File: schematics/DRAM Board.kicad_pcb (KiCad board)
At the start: 2 copper layers, 114.3 x 53.3 mm, 17 parts, among them U1 AS4C256K16E0, U16 44256_DRAM, U17 44256_DRAM, U18 44256_DRAM, U19 44256_DRAM, U2 AS4C256K16E0, U20 44256_DRAM, U21 44256_DRAM, U22 44256_DRAM, U23 44256_DRAM, U3 AS4C256K16E0, U4 AS4C256K16E0, U5 LM1117-3.3

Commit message: Add files via upload
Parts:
- removed U16, U17, U18, U19, U20, U21, U22, U23: 44256_DRAM, Package_DIP:DIP-20_W7.62mm_Socket
- removed U3, U4: AS4C256K16E0, Package_SO:TSOP-II-40-44_10.16x18.41mm_P0.8mm
- removed U5: LM1117-3.3, Package_TO_SOT_SMD:SOT-223
- added /bras0: Conn_01x01, Connector_PinHeader_2.54mm:PinHeader_1x01_P2.54mm_Vertical, F.Cu at (143.0, 82.1)
- added /bras1: Conn_01x01, Connector_PinHeader_2.54mm:PinHeader_1x01_P2.54mm_Vertical, F.Cu at (230.4, 82.0)
- added /lcas: Conn_01x01, Connector_PinHeader_2.54mm:PinHeader_1x01_P2.54mm_Vertical, F.Cu at (238.0, 82.0)
- added /ucas: Conn_01x01, Connector_PinHeader_2.54mm:PinHeader_1x01_P2.54mm_Vertical, F.Cu at (150.6, 82.1)
- added /we: Conn_01x01, Connector_PinHeader_2.54mm:PinHeader_1x01_P2.54mm_Vertical, F.Cu at (143.0, 79.6)
- added C5: 0.1uF, Capacitor_SMD:C_1206_3216Metric_Pad1.42x1.75mm_HandSolder, F.Cu at (215.9, 97.2)
- added C6: 0.1uF, Capacitor_SMD:C_1206_3216Metric_Pad1.42x1.75mm_HandSolder, F.Cu at (208.9, 80.6)
- added a0: Conn_01x01, Connector_PinHeader_2.54mm:PinHeader_1x01_P2.54mm_Vertical, F.Cu at (143.0, 87.2)
- added a1: Conn_01x01, Connector_PinHeader_2.54mm:PinHeader_1x01_P2.54mm_Vertical, F.Cu at (143.0, 89.7)
- added a2: Conn_01x01, Connector_PinHeader_2.54mm:PinHeader_1x01_P2.54mm_Vertical, F.Cu at (143.0, 92.3)
- added a3: Conn_01x01, Connector_PinHeader_2.54mm:PinHeader_1x01_P2.54mm_Vertical, F.Cu at (143.0, 94.8)
- added a4: Conn_01x01, Connector_PinHeader_2.54mm:PinHeader_1x01_P2.54mm_Vertical, F.Cu at (150.6, 97.3)
- added a5: Conn_01x01, Connector_PinHeader_2.54mm:PinHeader_1x01_P2.54mm_Vertical, F.Cu at (150.6, 94.8)
- added a6: Conn_01x01, Connector_PinHeader_2.54mm:PinHeader_1x01_P2.54mm_Vertical, F.Cu at (150.6, 92.3)
- added a7: Conn_01x01, Connector_PinHeader_2.54mm:PinHeader_1x01_P2.54mm_Vertical, F.Cu at (150.6, 89.7)
- added a8: Conn_01x01, Connector_PinHeader_2.54mm:PinHeader_1x01_P2.54mm_Vertical, F.Cu at (150.6, 87.2)
- added d0: Conn_01x01, Connector_PinHeader_2.54mm:PinHeader_1x01_P2.54mm_Vertical, F.Cu at (238.0, 79.5)
- added d1: Conn_01x01, Connector_PinHeader_2.54mm:PinHeader_1x01_P2.54mm_Vertical, F.Cu at (230.4, 77.0)
- added d10: Conn_01x01, Connector_PinHeader_2.54mm:PinHeader_1x01_P2.54mm_Vertical, F.Cu at (176.0, 77.0)
- added d11: Conn_01x01, Connector_PinHeader_2.54mm:PinHeader_1x01_P2.54mm_Vertical, F.Cu at (168.4, 74.5)
- added d12: Conn_01x01, Connector_PinHeader_2.54mm:PinHeader_1x01_P2.54mm_Vertical, F.Cu at (150.6, 79.6)
- added d13: Conn_01x01, Connector_PinHeader_2.54mm:PinHeader_1x01_P2.54mm_Vertical, F.Cu at (143.0, 77.0)
- added d14: Conn_01x01, Connector_PinHeader_2.54mm:PinHeader_1x01_P2.54mm_Vertical, F.Cu at (150.6, 77.0)
- added d15: Conn_01x01, Connector_PinHeader_2.54mm:PinHeader_1x01_P2.54mm_Vertical, F.Cu at (143.0, 74.5)
- added d2: Conn_01x01, Connector_PinHeader_2.54mm:PinHeader_1x01_P2.54mm_Vertical, F.Cu at (238.0, 77.0)
- added d3: Conn_01x01, Connector_PinHeader_2.54mm:PinHeader_1x01_P2.54mm_Vertical, F.Cu at (230.4, 74.4)
- added d4: Conn_01x01, Connector_PinHeader_2.54mm:PinHeader_1x01_P2.54mm_Vertical, F.Cu at (201.3, 79.5)
- added d5: Conn_01x01, Connector_PinHeader_2.54mm:PinHeader_1x01_P2.54mm_Vertical, F.Cu at (193.7, 76.9)
- added d6: Conn_01x01, Connector_PinHeader_2.54mm:PinHeader_1x01_P2.54mm_Vertical, F.Cu at (201.3, 76.9)
- added d7: Conn_01x01, Connector_PinHeader_2.54mm:PinHeader_1x01_P2.54mm_Vertical, F.Cu at (193.7, 74.4)
- added d8: Conn_01x01, Connector_PinHeader_2.54mm:PinHeader_1x01_P2.54mm_Vertical, F.Cu at (176.0, 79.6)
- added d9: Conn_01x01, Connector_PinHeader_2.54mm:PinHeader_1x01_P2.54mm_Vertical, F.Cu at (168.4, 77.0)
- added gnd_u17: Conn_01x01, Connector_PinHeader_2.54mm:PinHeader_1x01_P2.54mm_Vertical, F.Cu at (201.3, 74.4)
- added gnd_u19: Conn_01x01, Connector_PinHeader_2.54mm:PinHeader_1x01_P2.54mm_Vertical, F.Cu at (150.6, 74.5)
- added gnd_u20: Conn_01x01, Connector_PinHeader_2.54mm:PinHeader_1x01_P2.54mm_Vertical, F.Cu at (238.0, 74.4)
- added gnd_u23: Conn_01x01, Connector_PinHeader_2.54mm:PinHeader_1x01_P2.54mm_Vertical, F.Cu at (162.1, 74.5)
- added vcc_u17: Conn_01x01, Connector_PinHeader_2.54mm:PinHeader_1x01_P2.54mm_Vertical, F.Cu at (193.7, 97.3)
- added vcc_u19: Conn_01x01, Connector_PinHeader_2.54mm:PinHeader_1x01_P2.54mm_Vertical, F.Cu at (143.0, 97.3)
- added vcc_u20: Conn_01x01, Connector_PinHeader_2.54mm:PinHeader_1x01_P2.54mm_Vertical, F.Cu at (230.4, 97.3)
- added vcc_u23: Conn_01x01, Connector_PinHeader_2.54mm:PinHeader_1x01_P2.54mm_Vertical, F.Cu at (154.4, 97.3)
- U1, U2: value AS4C256K16E0 -> IS41C16257; footprint Package_SO:TSOP-II-40-44_10.16x18.41mm_P0.8mm -> Package_SO_J-Lead:SOJ-40
- moved C3 53.1 mm to (168.9, 80.6)
- moved C2 39.6 mm to (175.3, 97.2), turned to 180 degrees
- moved C4 38.6 mm to (209.6, 97.2)
- moved U1 34.1 mm to (172.7, 88.9)
- moved C1 32.8 mm to (168.9, 97.2)
- moved U2 31.8 mm to (213.4, 88.9)
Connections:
- C1 pad 1: /VCC -> /vcc5
- C2 pad 1: /VCC -> /vcc5
- C3 pad 1: /VCC -> /vcc5
- C4 pad 1: /VCC -> /vcc5
- U1 pad 1: /VCC -> /vcc5
- U1 pad 13: Net-(U1-Pad13) -> /_we
- U1 pad 14: Net-(U1-Pad14) -> /_bras0
- U1 pad 15: /_we -> Net-(U1-Pad15)
- U1 pad 16: /_bras0 -> /a0
- U1 pad 17: Net-(U1-Pad17) -> /a1
- U1 pad 18: /a0 -> /a2
- U1 pad 19: /a1 -> /a3
- U1 pad 20: /a2 -> /vcc5
- U1 pad 21: /a3 -> /gnd
- U1 pad 22: /VCC -> /a4
- U1 pad 23: /gnd -> /a5
- U1 pad 24: /a4 -> /a6
- U1 pad 25: /a5 -> /a7
- U1 pad 26: /a6 -> /a8
- U1 pad 27: /a7 -> /gnd
- U1 pad 28: /a8 -> /_ucas
- U1 pad 29: /_oe -> /_lcas
- U1 pad 30: /_ucas -> Net-(U1-Pad30)
- U1 pad 31: /_lcas -> /d8
- U1 pad 32: Net-(U1-Pad32) -> /d9
- U1 pad 35: /d8 -> /gnd
- U1 pad 36: /d9 -> /d12
- U1 pad 37: /d10 -> /d13
- U1 pad 38: /d11 -> /d14
- U1 pad 39: /gnd -> /d15
- U1 pad 40: /d12 -> /gnd
- U1 pad 6: /VCC -> /vcc5
- U2 pad 1: /VCC -> /vcc5
- U2 pad 13: Net-(U2-Pad13) -> /_we
- U2 pad 14: Net-(U2-Pad14) -> /_bras1
- U2 pad 15: /_we -> Net-(U2-Pad15)
- U2 pad 16: /_bras0 -> /a0
- U2 pad 17: Net-(U2-Pad17) -> /a1
- U2 pad 18: /a0 -> /a2
- U2 pad 19: /a1 -> /a3
- U2 pad 20: /a2 -> /vcc5
- U2 pad 21: /a3 -> /gnd
- U2 pad 22: /VCC -> /a4
- U2 pad 23: /gnd -> /a5
- U2 pad 24: /a4 -> /a6
- U2 pad 25: /a5 -> /a7
- U2 pad 26: /a6 -> /a8
- U2 pad 27: /a7 -> /gnd
- U2 pad 28: /a8 -> /_ucas
- U2 pad 29: /_oe -> /_lcas
- U2 pad 30: /_ucas -> Net-(U2-Pad30)
- U2 pad 31: /_lcas -> /d8
- U2 pad 32: Net-(U2-Pad32) -> /d9
- U2 pad 35: /d8 -> /gnd
- U2 pad 36: /d9 -> /d12
- U2 pad 37: /d10 -> /d13
- U2 pad 38: /d11 -> /d14
- U2 pad 39: /gnd -> /d15
- U2 pad 40: /d12 -> /gnd
- U2 pad 6: /VCC -> /vcc5
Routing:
- net /_oe: track 182.9 -> 0.00 mm, vias 3 -> 0
- net /VCC: track 180.0 -> 0.00 mm, vias 5 -> 0
- net /a0: track 223.4 -> 87.9 mm, vias 3 -> 1
- net /a2: track 222.0 -> 88.9 mm, vias 2 -> 1
- net /a8: track 200.2 -> 77.4 mm, vias 3 -> 0
- net /a6: track 202.9 -> 82.0 mm, vias 2 -> 0
- net /a7: track 190.7 -> 79.7 mm, vias 3 -> 0
- net /a5: track 186.9 -> 84.3 mm, vias 5 -> 0
- net /_bras1: track 118.9 -> 18.4 mm, vias 3 -> 0
- net /_we: track 182.4 -> 84.5 mm, vias 4 -> 1
- net /a4: track 180.9 -> 84.8 mm, vias 5 -> 0
- net /gnd: track 292.2 -> 207.3 mm, vias 5 -> 8
- net /_bras0: track 123.7 -> 40.0 mm, vias 3 -> 1
- net /a3: track 222.6 -> 150.8 mm, vias 2 -> 1
- net /d14: track 136.6 -> 76.4 mm, vias 3 -> 1
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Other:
- board size 114.3 x 53.3 mm -> 99.1 x 27.9 mm
- board text added: "IS41C16257"
- board text added: "gnd"
- board text added: "vcc"

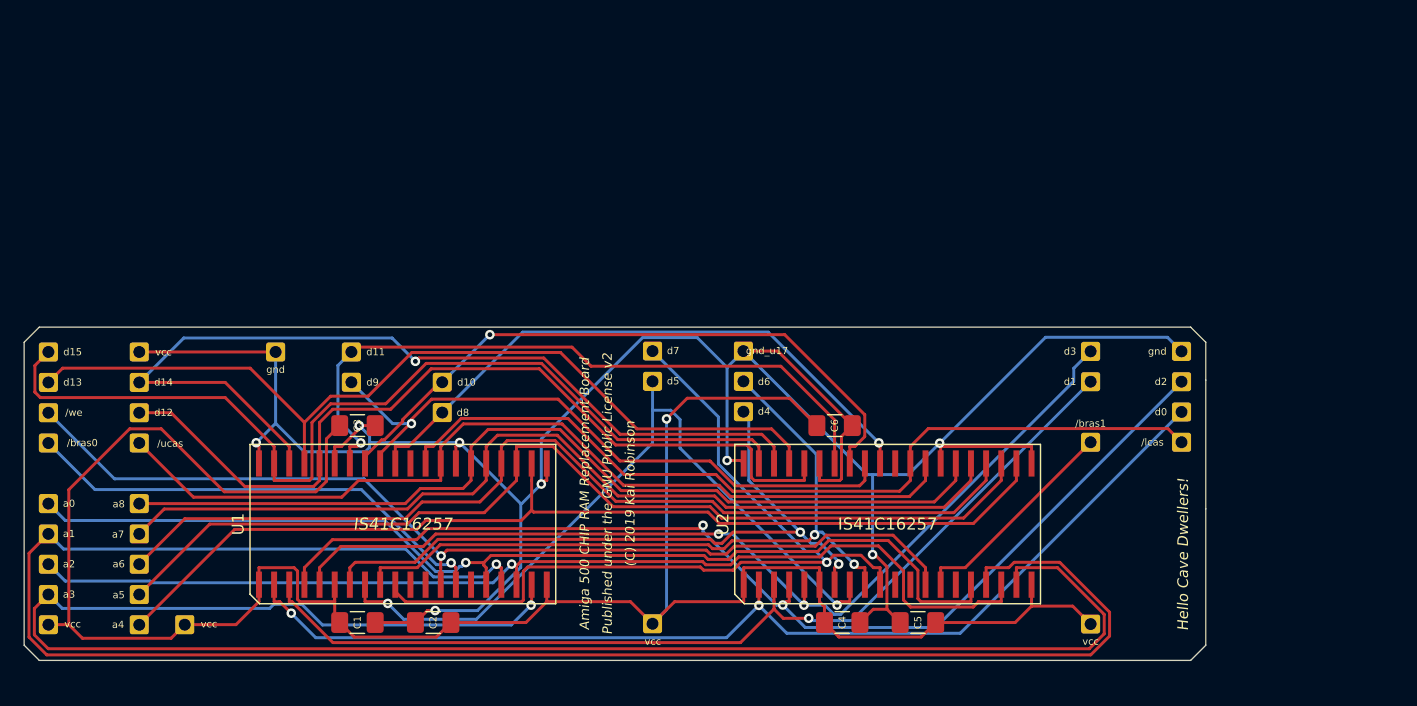
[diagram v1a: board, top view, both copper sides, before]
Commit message: Re-doing the copper fill
Switched copper fill to GND for both sides
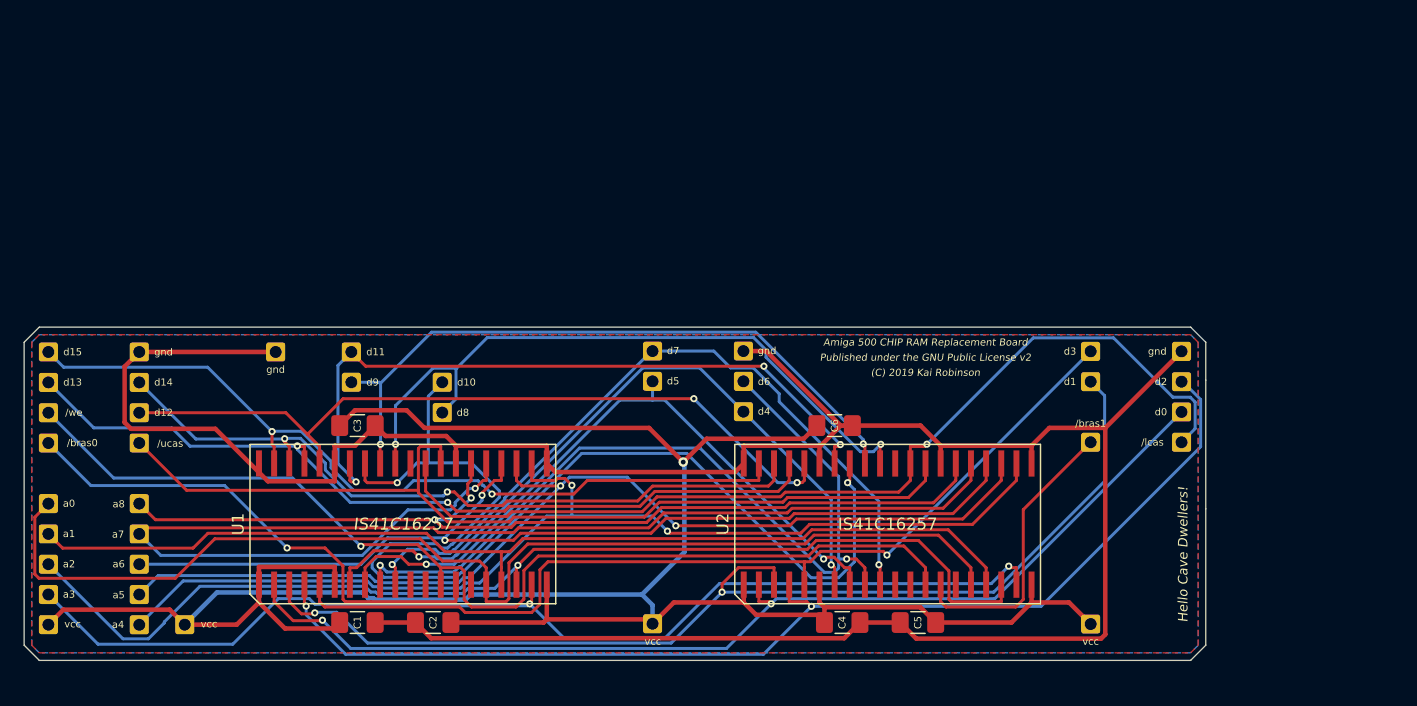
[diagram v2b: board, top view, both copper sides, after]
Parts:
- renumbered gnd_u17 to gnd
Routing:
- net /a1: track 158.3 -> 86.5 mm, vias 1 -> 0
- net /a3: track 150.8 -> 91.6 mm, vias 1 -> 2
- net /d10: track 54.4 -> 94.4 mm, vias 1 -> 2
- net /a7: track 79.7 -> 107.3 mm, vias 0 -> 1
- net /vcc5: track 188.0 -> 203.4 mm
- net /d14: track 76.4 -> 62.7 mm, vias 1 -> 2
- net /gnd: track 207.3 -> 218.9 mm, vias 8 -> 0
- net /d1: track 81.9 -> 92.8 mm, vias 1 -> 2
- net /d6: track 61.4 -> 71.9 mm
- net /d15: track 80.4 -> 70.2 mm, vias 0 -> 2
- net /_lcas: track 72.6 -> 81.7 mm, vias 0 -> 1
- net /a0: track 87.9 -> 96.9 mm, vias 1 -> 0
- net /d7: track 70.9 -> 63.0 mm, vias 1 -> 2
- net /d12: track 71.9 -> 65.0 mm, vias 0 -> 2
- net /d8: track 51.6 -> 58.3 mm, vias 1 -> 2
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- added copper zone on B.Cu, net /gnd
- added copper zone on F.Cu, net /gnd
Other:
- net class Default: via_dia 0.8 -> 0.6; via_drill 0.4 -> 0.3
- net class Power added: clearance 0.2, trace_width 0.381, via_dia 0.8, via_drill 0.4
- rule trace_min: 0.2 -> 0.1
- rule via_min_drill: 0.3 -> 0.2
